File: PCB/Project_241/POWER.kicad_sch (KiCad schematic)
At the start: 14 parts, among them J6 BATT_CONN, U6 XL1509-5.0, U7 RT9013

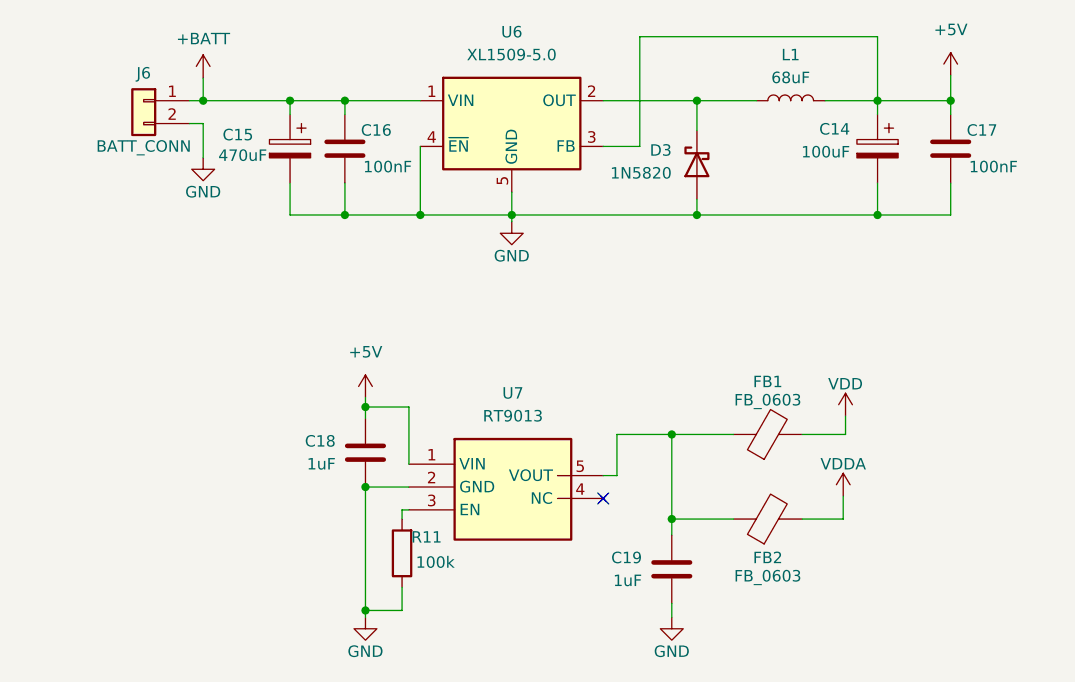
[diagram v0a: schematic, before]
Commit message: update schematic
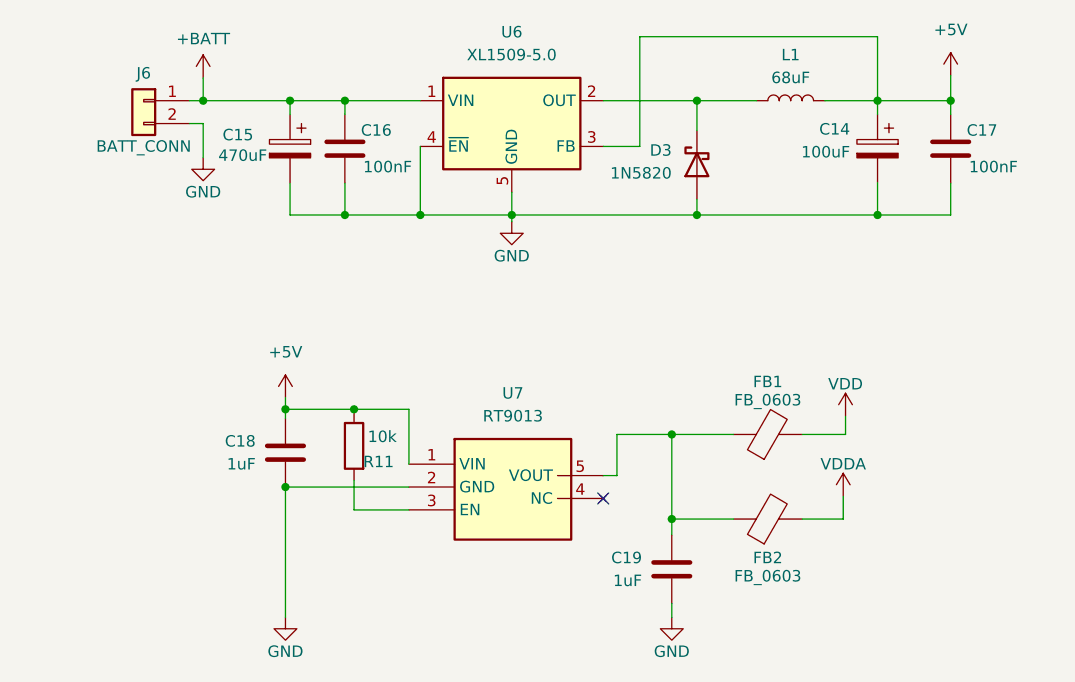
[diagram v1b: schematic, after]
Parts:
- R11: value 100k -> 10k
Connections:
- net +5V: now also R11.1
- net GND: no longer R11.1
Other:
- moved on the sheet: C18, R11
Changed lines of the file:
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@@
-	)
-	(junction
-		(at 124.206 114.554)
-		(diameter 0)
-		(color 0 0 0 0)
 	)
 	(junction
@@
 	)
 	(junction
+		(at 122.936 114.808)
+		(diameter 0)
+		(color 0 0 0 0)
+	)
+	(junction
 		(at 121.92 80.518)
 		(diameter 0)
@@
 	)
 	(junction
-		(at 124.206 123.444)
+		(at 115.316 123.444)
+		(diameter 0)
+		(color 0 0 0 0)
+	)
+	(junction
+		(at 115.316 114.808)
 		(diameter 0)
 		(color 0 0 0 0)
@@
 		(color 0 0 0 0)
 	)
-	(junction
-		(at 124.206 137.16)
-		(diameter 0)
-		(color 0 0 0 0)
-	)
 	(no_connect
 		(at 150.622 124.714)
@@
 	(wire
 		(pts
+			(xy 122.936 115.062) (xy 122.936 114.808)
+		)
+		(stroke
+			(width 0)
+			(type default)
+		)
+	)
+	(wire
+		(pts
 			(xy 181.102 82.042) (xy 181.102 80.518)
 		)
@@
 	(wire
 		(pts
+			(xy 122.936 114.808) (xy 129.032 114.808)
+		)
+		(stroke
+			(width 0)
+			(type default)
+		)
+	)
+	(wire
+		(pts
 			(xy 167.64 80.518) (xy 161.036 80.518)
 		)
@@
 	(wire
 		(pts
-			(xy 129.032 114.554) (xy 124.206 114.554)
-		)
-		(stroke
-			(width 0)
-			(type default)
-		)
-	)
-	(wire
-		(pts
-			(xy 124.206 137.16) (xy 124.206 123.444)
-		)
-		(stroke
-			(width 0)
-			(type default)
-		)
-	)
-	(wire
-		(pts
-			(xy 128.27 125.984) (xy 129.032 125.984)
+			(xy 115.316 114.808) (xy 122.936 114.808)
+		)
+		(stroke
+			(width 0)
+			(type default)
+		)
+	)
+	(wire
+		(pts
+			(xy 115.316 123.444) (xy 115.316 137.922)
+		)
+		(stroke
+			(width 0)
+			(type default)
+		)
+	)
+	(wire
+		(pts
+			(xy 122.936 125.984) (xy 129.032 125.984)
 		)
 		(stroke
@@
 	(wire
 		(pts
-			(xy 124.206 113.538) (xy 124.206 114.554)
-		)
-		(stroke
-			(width 0)
-			(type default)
-		)
-	)
-	(wire
-		(pts
 			(xy 106.172 80.518) (xy 115.824 80.518)
 		)
@@
 	(wire
 		(pts
-			(xy 128.27 127) (xy 128.27 125.984)
+			(xy 122.936 122.682) (xy 122.936 125.984)
 		)
 		(stroke
@@
 	(wire
 		(pts
-			(xy 128.27 137.16) (xy 124.206 137.16)
-		)
-		(stroke
-			(width 0)
-			(type default)
-		)
-	)
-	(wire
-		(pts
-			(xy 129.032 120.904) (xy 129.032 114.554)
-		)
-		(stroke
-			(width 0)
-			(type default)
-		)
-	)
-	(wire
-		(pts
 			(xy 154.686 85.598) (xy 154.686 73.406)
 		)
@@
 	(wire
 		(pts
+			(xy 129.032 114.808) (xy 129.032 120.904)
+		)
+		(stroke
+			(width 0)
+			(type default)
+		)
+	)
+	(wire
+		(pts
 			(xy 150.622 85.598) (xy 154.686 85.598)
 		)
@@
 	(wire
 		(pts
-			(xy 124.206 123.444) (xy 129.032 123.444)
+			(xy 115.316 123.444) (xy 129.032 123.444)
 		)
 		(stroke
@@
 	(wire
 		(pts
-			(xy 124.206 114.554) (xy 124.206 115.824)
-		)
-		(stroke
-			(width 0)
-			(type default)
-		)
-	)
-	(wire
-		(pts
 			(xy 106.172 86.868) (xy 106.172 83.058)
 		)
@@
 	(wire
 		(pts
+			(xy 115.316 113.538) (xy 115.316 114.808)
+		)
+		(stroke
+			(width 0)
+			(type default)
+		)
+	)
+	(wire
+		(pts
 			(xy 177.546 115.57) (xy 177.546 117.602)
 		)
@@
 	(wire
 		(pts
+			(xy 115.316 114.808) (xy 115.316 115.824)
+		)
+		(stroke
+			(width 0)
+			(type default)
+		)
+	)
+	(wire
+		(pts
 			(xy 181.102 73.406) (xy 181.102 80.518)
 		)
@@
 	(wire
 		(pts
-			(xy 128.27 134.62) (xy 128.27 137.16)
-		)
-		(stroke
-			(width 0)
-			(type default)
-		)
-	)
-	(wire
-		(pts
 			(xy 140.462 90.678) (xy 140.462 93.218)
 		)
@@
 		(pts
 			(xy 189.23 77.724) (xy 189.23 80.518)
-		)
-		(stroke
-			(width 0)
-			(type default)
-		)
-	)
-	(wire
-		(pts
-			(xy 124.206 137.922) (xy 124.206 137.16)
 		)
 		(stroke
@@
 	(symbol
 		(lib_id "Device:R")
-		(at 128.27 130.81 180)
+		(at 122.936 118.872 0)
+		(mirror y)
 		(unit 1)
 		(exclude_from_sim no)
@@
 		(dnp no)
 		(property "Reference" "R11"
-			(at 129.286 129.032 0)
+			(at 123.952 120.65 0)
 			(effects
 				(font
@@
 			)
 		)
-		(property "Value" "100k"
-			(at 129.794 131.826 0)
+		(property "Value" "10k"
+			(at 124.46 117.856 0)
 			(effects
 				(font
@@
 		)
 		(property "Footprint" ""
-			(at 130.048 130.81 90)
+			(at 124.714 118.872 90)
 			(effects
 				(font
@@
 		)
 		(property "Datasheet" "~"
-			(at 128.27 130.81 0)
+			(at 122.936 118.872 0)
 			(effects
 				(font
@@
 		)
 		(property "Description" "Resistor"
-			(at 128.27 130.81 0)
+			(at 122.936 118.872 0)
 			(effects
 				(font
@@
 	(symbol
 		(lib_id "power:+5V")
-		(at 124.206 113.538 0)
+		(at 115.316 113.538 0)
 		(unit 1)
 		(exclude_from_sim no)
@@
 		(fields_autoplaced yes)
 		(property "Reference" "#PWR035"
-			(at 124.206 117.348 0)
+			(at 115.316 117.348 0)
 			(effects
 				(font
@@
 		)
 		(property "Value" "+5V"
-			(at 124.206 108.458 0)
+			(at 115.316 108.458 0)
 			(effects
 				(font
@@
 		)
 		(property "Footprint" ""
-			(at 124.206 113.538 0)
+			(at 115.316 113.538 0)
 			(effects
 				(font
@@
 		)
 		(property "Datasheet" ""
-			(at 124.206 113.538 0)
+			(at 115.316 113.538 0)
 			(effects
 				(font
@@
 		)
 		(property "Description" "Power symbol creates a global label with name \"+5V\""
-			(at 124.206 113.538 0)
+			(at 115.316 113.538 0)
 			(effects
 				(font
@@
 	(symbol
 		(lib_id "power:GND")
-		(at 124.206 137.922 0)
+		(at 115.316 137.922 0)
 		(unit 1)
 		(exclude_from_sim no)
@@
 		(dnp no)
 		(property "Reference" "#PWR034"
-			(at 124.206 144.272 0)
+			(at 115.316 144.272 0)
 			(effects
 				(font
@@
 		)
 		(property "Value" "GND"
-			(at 124.206 141.732 0)
+			(at 115.316 141.732 0)
 			(effects
 				(font
@@
 		)
 		(property "Footprint" ""
-			(at 124.206 137.922 0)
+			(at 115.316 137.922 0)
 			(effects
 				(font
@@
 		)
 		(property "Datasheet" ""
-			(at 124.206 137.922 0)
+			(at 115.316 137.922 0)
 			(effects
 				(font
@@
 		)
 		(property "Description" "Power symbol creates a global label with name \"GND\" , ground"
-			(at 124.206 137.922 0)
+			(at 115.316 137.922 0)
 			(effects
 				(font
@@
 	(symbol
 		(lib_id "Device:C")
-		(at 124.206 119.634 0)
+		(at 115.316 119.634 0)
 		(unit 1)
 		(exclude_from_sim no)
@@
 		(dnp no)
 		(property "Reference" "C18"
-			(at 120.904 118.3639 0)
+			(at 112.014 118.3639 0)
 			(effects
 				(font
@@
 		)
 		(property "Value" "1uF"
-			(at 120.904 120.9039 0)
+			(at 112.014 120.9039 0)
 			(effects
 				(font
@@
 		)
 		(property "Footprint" ""
-			(at 125.1712 123.444 0)
+			(at 116.2812 123.444 0)
 			(effects
 				(font
@@
 		)
 		(property "Datasheet" "~"
-			(at 124.206 119.634 0)
+			(at 115.316 119.634 0)
 			(effects
 				(font
@@
 		)
 		(property "Description" "Unpolarized capacitor"
-			(at 124.206 119.634 0)
-			(effects
-				(font
+			(at 115.316 119.634 0)
+			(effects
+				(font

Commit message: update schematic
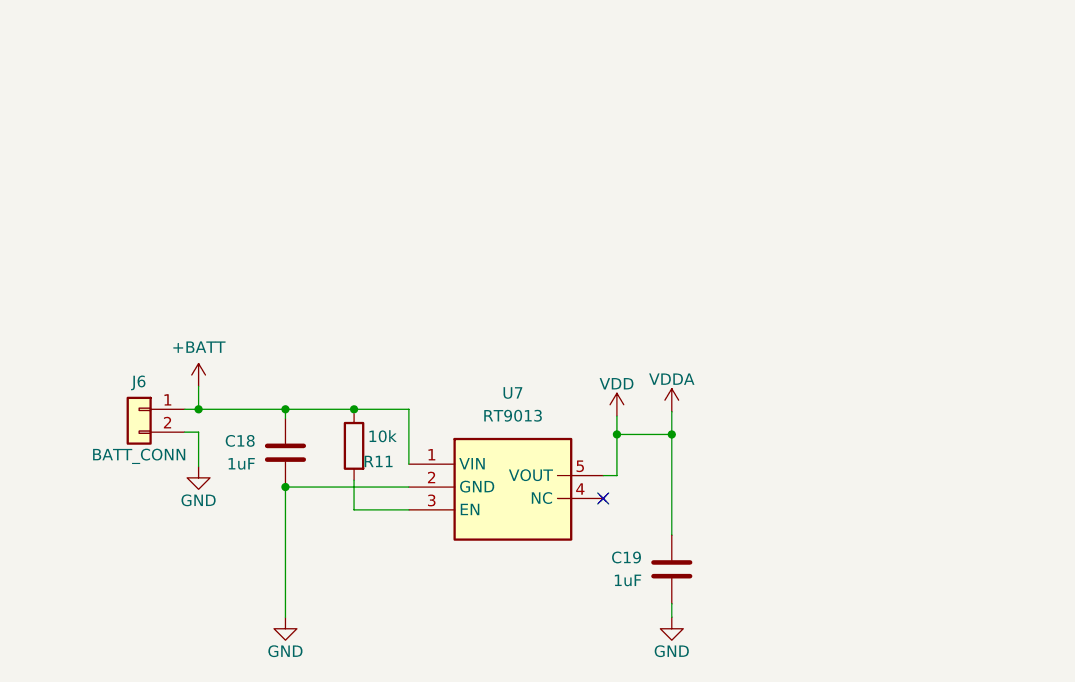
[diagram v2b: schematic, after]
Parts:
- removed C14: 100uF, symbol Device:C_Polarized
- removed C15: 470uF, symbol Device:C_Polarized
- removed C16, C17: 100nF, symbol Device:C
- removed D3: 1N5820, symbol Device:D_Schottky
- removed FB1, FB2: FB_0603, symbol Device:FerriteBead
- removed L1: 68uF, symbol Device:L
- removed U6: XL1509-5.0, Package_SO:SOIC-8_3.9x4.9mm_P1.27mm, symbol Regulator_Switching:XL1509-5.0
- C18, C19: footprint (none) -> Capacitor_SMD:C_0603_1608Metric
- J6: footprint (none) -> IVSFootprint:XH_2P_2.54mm_Horizontal_SMD
- R11: footprint (none) -> Resistor_SMD:R_0603_1608Metric
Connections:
- net +5V is gone; now on net +BATT: C18.1, R11.1, U7.1 (VIN)
- net VDD: now also C19.1, U7.5 (VOUT)
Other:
- moved on the sheet: J6

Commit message: update gerber
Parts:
- removed R11: 10k, Resistor_SMD:R_0603_1608Metric, symbol Device:R
- added C17: 10uF, Capacitor_SMD:C_0603_1608Metric, symbol Device:C
- added C20, C21: 100nF, Capacitor_SMD:C_0603_1608Metric, symbol Device:C
- added D3: PWR_LED, LED_SMD:LED_0603_1608Metric, symbol Device:LED
- added F1: 1A, Fuse:Fuse_0805_2012Metric, symbol Device:Polyfuse_Small
- added R8: 100R, Resistor_SMD:R_0603_1608Metric, symbol Device:R_Small
- J6: footprint IVSFootprint:XH_2P_2.54mm_Horizontal_SMD -> IVSFootprint:XH 2.54 2Pin Female
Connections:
- net +BATT: now also U7.3 (EN), C17.1, C20.1, F1.2; no longer J6.1 (Pin_1)
- net GND: now also C17.2, C20.2, C21.2, D3.1 (K)
- net VDD: now also C21.1, R8.1
- new net: D3.2 (A), R8.2
- new net: F1.1, J6.1 (Pin_1)
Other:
- moved on the sheet: C18, C19, J6, U7
